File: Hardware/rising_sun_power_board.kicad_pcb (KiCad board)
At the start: 4 copper layers, 38.1 x 63.5 mm, 32 parts, among them J1 Barrel_Jack, J2 Conn_01x03_Socket, J3 Conn_01x03_Socket, SW1 SW_Push, SW2 SW_Push, U1 ESP32, U2 MIC5219, U4 TXU0102DCUR, U5 UA78M05IDCYR

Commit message: Final rev1.0 version
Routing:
- net +5V: track 9.56 -> 15.5 mm
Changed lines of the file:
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@@
       (pts (xy 50.8 72.644) (xy 50.8 73.914))
       (height 3.048)
-      (gr_text "0.0500 in" (at 46.652 73.279 90) (layer "F.Fab")
+      (gr_text "1.2700 mm" (at 46.652 73.279 90) (layer "F.Fab")
         (effects (font (size 1 1) (thickness 0.1)))
       )
@@
       (pts (xy 74.93 73.914) (xy 74.93 14.986))
       (height 4.318)
-      (gr_text "2.3200 in" (at 78.148 44.45 90) (layer "F.Fab")
+      (gr_text "58.9280 mm" (at 78.148 44.45 90) (layer "F.Fab")
         (effects (font (size 1 1) (thickness 0.1)))
       )
@@
       (pts (xy 50.8 72.644) (xy 49.53 72.644))
       (height -6.858)
-      (gr_text "0.0500 in" (at 50.165 78.402) (layer "F.Fab")
+      (gr_text "1.2700 mm" (at 50.165 78.402) (layer "F.Fab")
         (effects (font (size 1 1) (thickness 0.1)))
       )
@@
       (pts (xy 49.53 73.914) (xy 74.93 73.914))
       (height 9.398)
-      (gr_text "1.0000 in" (at 62.23 82.212) (layer "F.Fab")
+      (gr_text "25.4000 mm" (at 62.23 82.212) (layer "F.Fab")
         (effects (font (size 1 1) (thickness 0.1)))
       )
@@
       (pts (xy 49.53 72.644) (xy 73.66 72.644))
       (height 8.636)
-      (gr_text "0.9500 in" (at 61.595 80.18) (layer "F.Fab")
+      (gr_text "24.1300 mm" (at 61.595 80.18) (layer "F.Fab")
         (effects (font (size 1 1) (thickness 0.1)))
       )
@@
   (via (at 60.96 53.975) (size 0.762) (drill 0.381) (layers "F.Cu" "B.Cu") (net 2))
   (via (at 69.215 37.465) (size 0.762) (drill 0.381) (layers "F.Cu" "B.Cu") (net 2))
+  (segment (start 67.056 34.036) (end 66.04 35.052) (width 0.1524) (layer "B.Cu") (net 2))
+  (segment (start 61.468 55.88) (end 61.468 57.658) (width 0.3048) (layer "B.Cu") (net 2))
+  (segment (start 61.468 57.658) (end 61.595 57.785) (width 0.3048) (layer "B.Cu") (net 2))
   (segment (start 61.1 55.875) (end 61.1 54.115) (width 0.3048) (layer "B.Cu") (net 2))
   (segment (start 61.1 54.115) (end 60.96 53.975) (width 0.3048) (layer "B.Cu") (net 2))
   (segment (start 65.265 35.065) (end 64.77 35.56) (width 0.3048) (layer "B.Cu") (net 2))
+  (segment (start 61.1 55.875) (end 61.463 55.875) (width 0.3048) (layer "B.Cu") (net 2))
   (segment (start 66.04 35.065) (end 65.265 35.065) (width 0.3048) (layer "B.Cu") (net 2))
   (segment (start 68.33 35.205) (end 68.33 36.58) (width 0.1524) (layer "B.Cu") (net 2))
   (segment (start 61.595 57.785) (end 59.69 57.785) (width 0.3048) (layer "B.Cu") (net 2))
+  (segment (start 61.463 55.875) (end 61.468 55.88) (width 0.3048) (layer "B.Cu") (net 2))
+  (segment (start 68.33 35.205) (end 68.33 34.6026) (width 0.1524) (layer "B.Cu") (net 2))
+  (segment (start 68.33 34.6026) (end 67.7634 34.036) (width 0.1524) (layer "B.Cu") (net 2))
+  (segment (start 66.04 35.052) (end 66.04 35.065) (width 0.1524) (layer "B.Cu") (net 2))
+  (segment (start 67.7634 34.036) (end 67.056 34.036) (width 0.1524) (layer "B.Cu") (net 2))
   (segment (start 63.805 67.31) (end 65.405 67.31) (width 0.3048) (layer "B.Cu") (net 2))
   (segment (start 68.33 36.58) (end 69.215 37.465) (width 0.1524) (layer "B.Cu") (net 2))
@@
   (segment (start 76.9329 36.83) (end 76.9329 28.0379) (width 0.3048) (layer "B.Cu") (net 11))
   (segment (start 66.675 27.94) (end 66.675 30.9524) (width 0.3048) (layer "B.Cu") (net 11))
-  (segment (start 77.5684 25.8096) (end 76.708 25.8096) (width 0.3048) (layer "F.Cu") (net 12))
+  (segment (start 67.7196 25.8096) (end 77.5684 25.8096) (width 0.3048) (layer "F.Cu") (net 12))
   (segment (start 66.8592 26.67) (end 61.595 26.67) (width 0.3048) (layer "F.Cu") (net 12))
   (segment (start 81.28 22.098) (end 77.5684 25.8096) (width 0.3048) (layer "F.Cu") (net 12))
-  (segment (start 76.708 25.8096) (end 67.7196 25.8096) (width 0.3048) (layer "F.Cu") (net 12))
   (segment (start 61.595 26.67) (end 60.325 27.94) (width 0.3048) (layer "F.Cu") (net 12))
   (segment (start 67.7196 25.8096) (end 66.8592 26.67) (width 0.3048) (layer "F.Cu") (net 12))
@@
   (via (at 55.88 27.94) (size 0.762) (drill 0.381) (layers "F.Cu" "B.Cu") (net 12))
   (via (at 81.28 22.098) (size 0.762) (drill 0.381) (layers "F.Cu" "B.Cu") (net 12))
-  (segment (start 85.52 23.46) (end 85.52 23.685) (width 0.3048) (layer "B.Cu") (net 12))
   (segment (start 54.61 27.94) (end 54.23 27.56) (width 0.3048) (layer "B.Cu") (net 12))
   (segment (start 84.383 22.098) (end 81.28 22.098) (width 0.3048) (layer "B.Cu") (net 12))
@@
   (via (at 55.245 25.4) (size 0.762) (drill 0.381) (layers "F.Cu" "B.Cu") (net 15))
   (via (at 85.52 17.78) (size 0.762) (drill 0.381) (layers "F.Cu" "B.Cu") (net 15))
-  (segment (start 85.52 20.39) (end 85.52 20.6198) (width 0.3048) (layer "B.Cu") (net 15))
   (segment (start 85.52 15.24) (end 85.52 17.78) (width 0.3048) (layer "B.Cu") (net 15))
   (segment (start 54.23 24.385) (end 55.245 25.4) (width 0.3048) (layer "B.Cu") (net 15))
   (segment (start 54.23 24.13) (end 53.976 24.384) (width 0.3048) (layer "B.Cu") (net 15))
-  (segment (start 85.52 20.39) (end 85.52 20.615) (width 0.3048) (layer "B.Cu") (net 15))
   (segment (start 54.23 24.13) (end 54.23 24.385) (width 0.3048) (layer "B.Cu") (net 15))
   (segment (start 53.976 24.384) (end 50.8 24.384) (width 0.3048) (layer "B.Cu") (net 15))

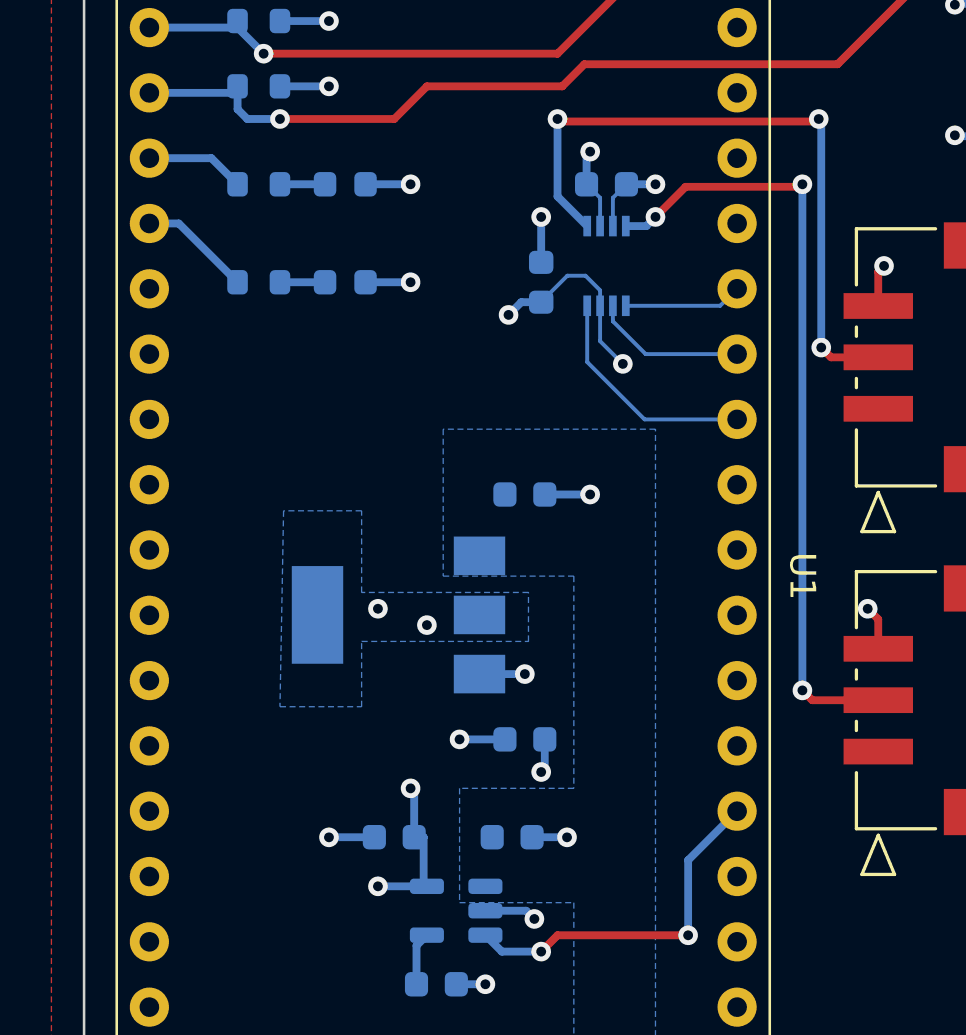
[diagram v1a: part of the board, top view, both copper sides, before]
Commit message: fixed some gpios connection
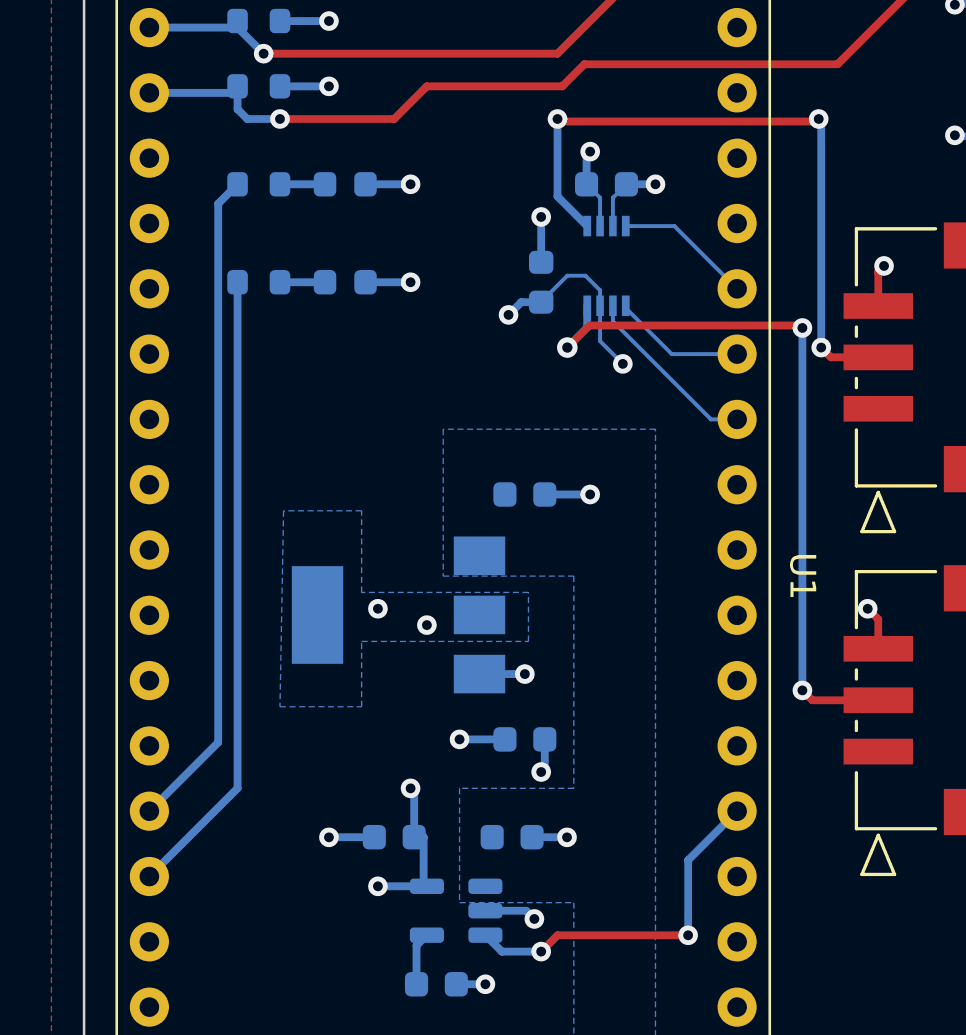
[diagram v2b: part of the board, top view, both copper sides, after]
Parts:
- U5: value UA78M05IDCYR -> UA78M33IDCYR
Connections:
- U1 pad 17: /GPIO_LED2 -> unconnected-(U1-39-Pad17)
- U1 pad 18: /GPIO_LED1 -> unconnected-(U1-38-Pad18)
- U1 pad 34: /LED_ENABLE_3V3_2 -> /LEVEL_SHIFT_EN
- U1 pad 35: /LEVEL_SHIFT_EN -> /LED_ENABLE_3V3_1
- U1 pad 36: /LED_ENABLE_3V3_1 -> /LED_ENABLE_3V3_2
- U1 pad 7: unconnected-(U1-13-Pad7) -> /GPIO_LED2
- U1 pad 8: unconnected-(U1-12-Pad8) -> /GPIO_LED1
- U4 pad 4: /LED_ENABLE_5V_1 -> /LED_ENABLE_3V3_2
- U4 pad 8: /LED_ENABLE_3V3_2 -> /LED_ENABLE_5V_1
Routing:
- net /GPIO_LED1: track 3.85 -> 25.8 mm
- net /GPIO_LED2: track 4.38 -> 24.5 mm
- net /LED_ENABLE_3V3_2: track 8.94 -> 5.34 mm
- net /LED_ENABLE_5V_1: track 30.3 -> 28.7 mm
- net /LEVEL_SHIFT_EN: track 5.96 -> 7.01 mm
- net /LED_ENABLE_3V3_1: track 4.60 -> 5.16 mm
